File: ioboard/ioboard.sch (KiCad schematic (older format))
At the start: 18 parts

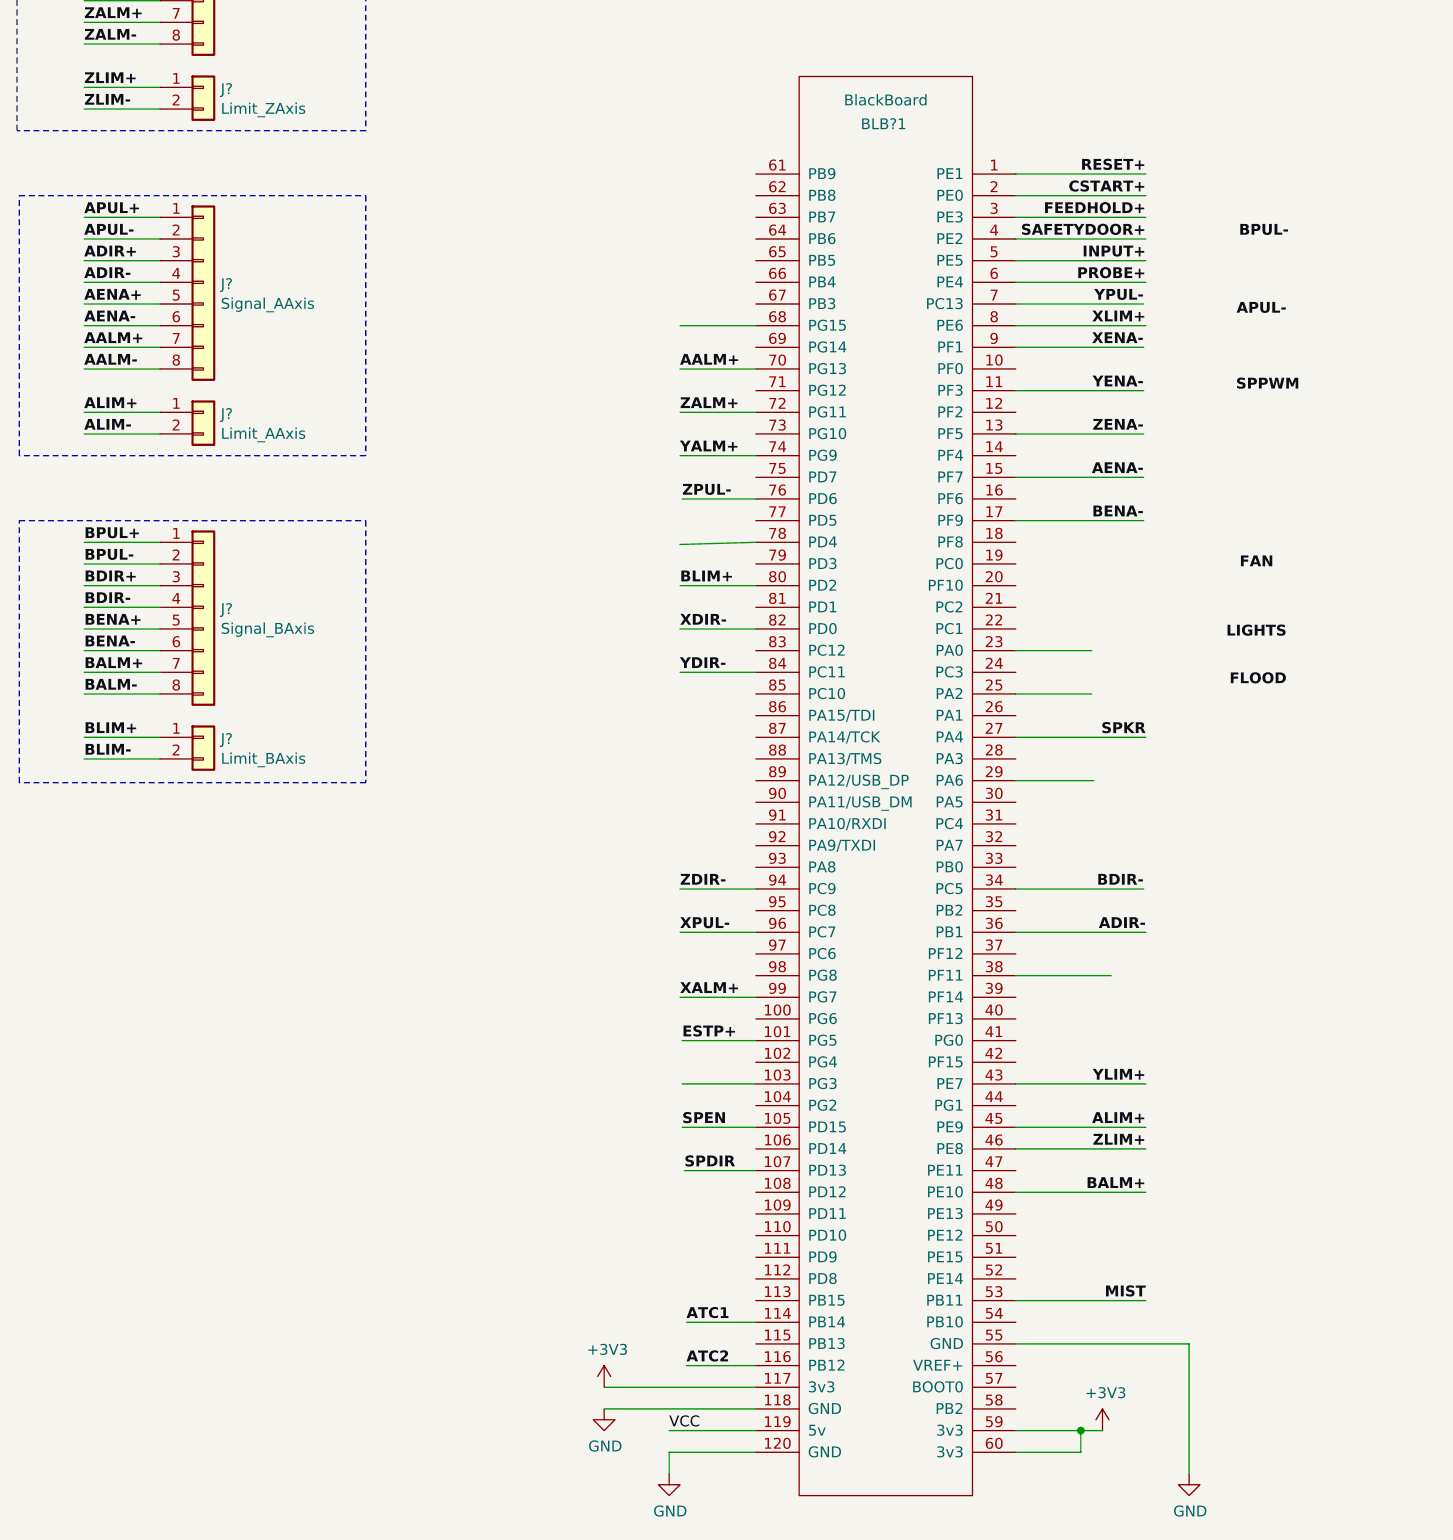
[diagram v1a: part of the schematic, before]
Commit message: system.stm32.[ch] has been ported and now compiles
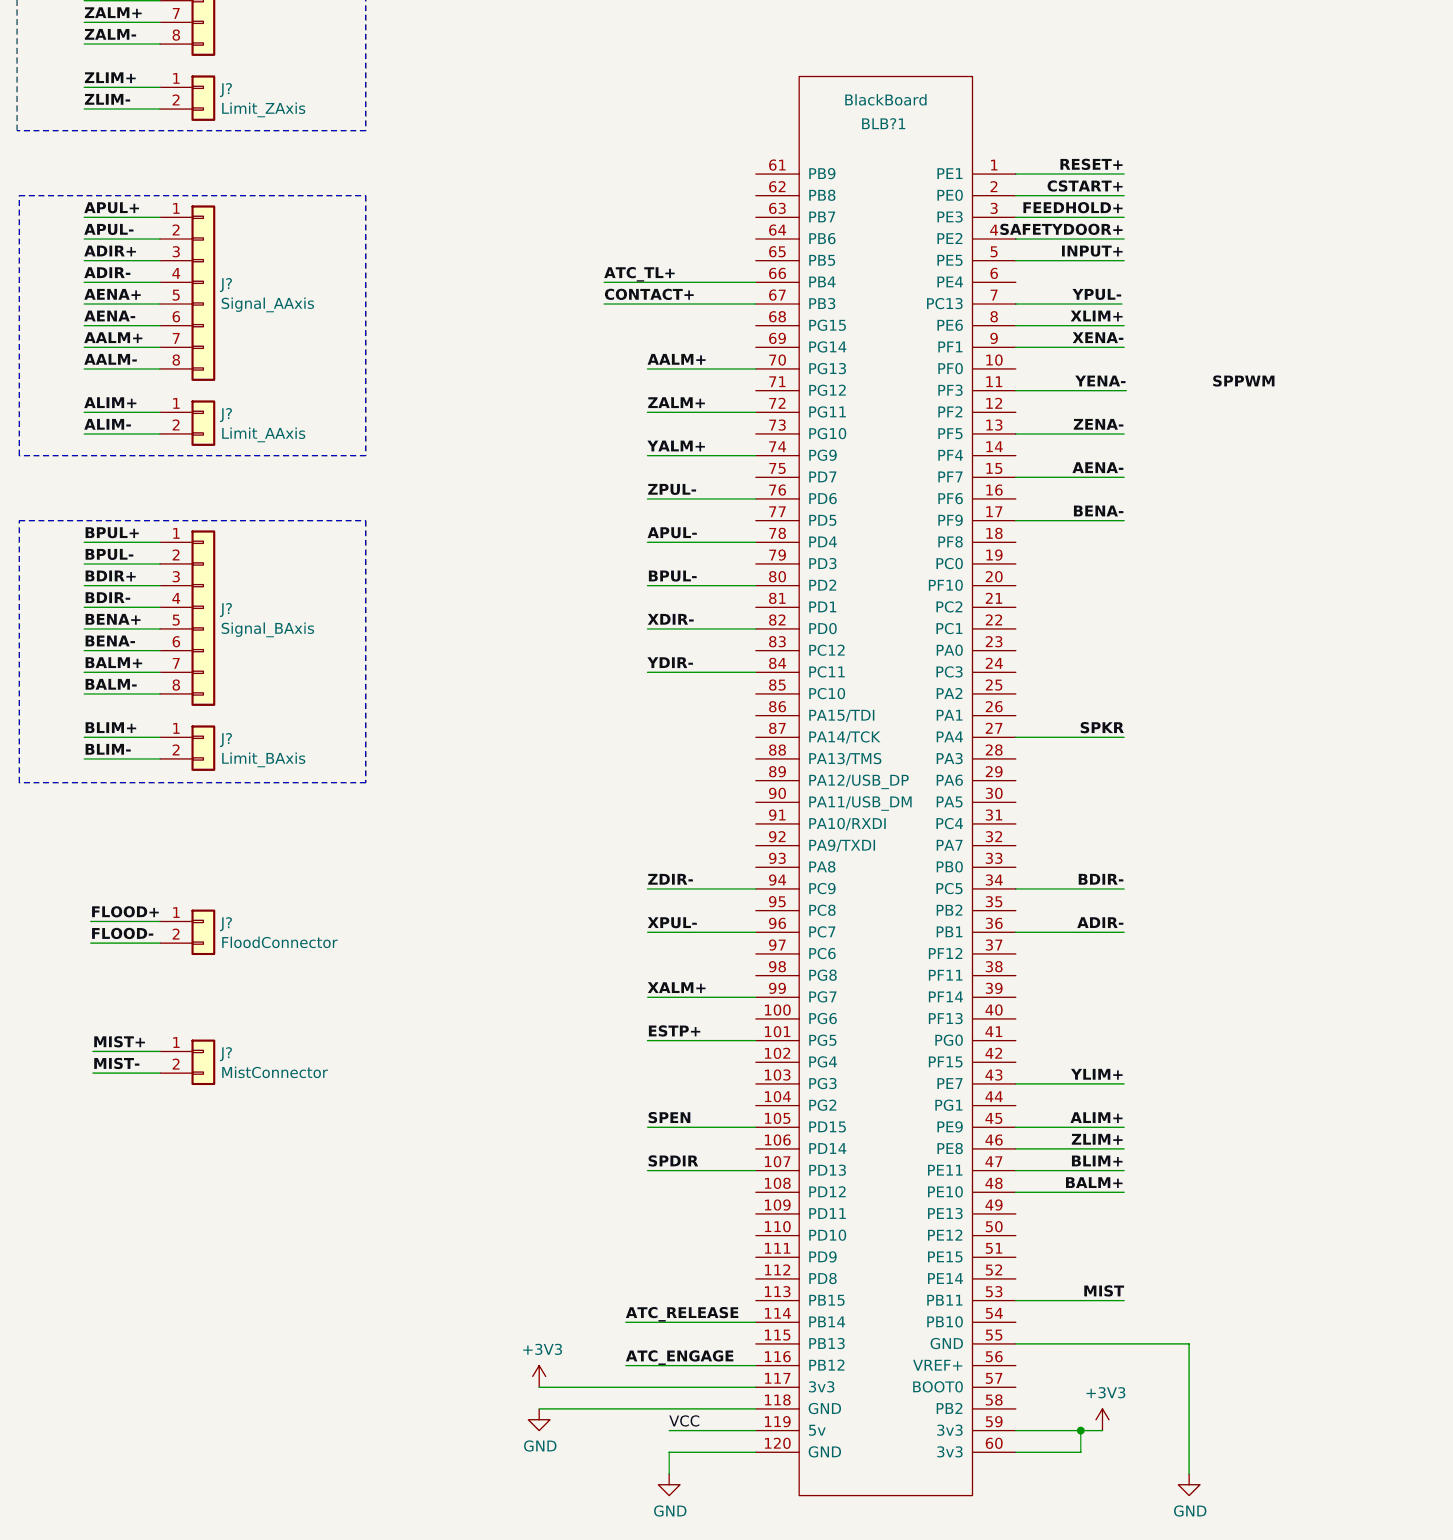
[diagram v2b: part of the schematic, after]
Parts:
- added J?: FloodConnector, symbol Connector_Generic:Conn_01x02
- added J?: MistConnector, symbol Connector_Generic:Conn_01x02
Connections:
- net labels added: ATC_ENGAGE, ATC_RELEASE, ATC_TL+, CONTACT+, FLOOD+, FLOOD-, MIST+, MIST-
- net labels removed: ATC1, ATC2, FAN, FLOOD, LIGHTS, PROBE+
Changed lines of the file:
@@
 L power:GND #PWR?
 U 1 1 606A4231
-P 4100 11500
-F 0 "#PWR?" H 4100 11250 50  0001 C CNN
-F 1 "GND" H 4105 11327 50  0000 C CNN
-F 2 "" H 4100 11500 50  0001 C CNN
-F 3 "" H 4100 11500 50  0001 C CNN
-	1    4100 11500
+P 3800 11500
+F 0 "#PWR?" H 3800 11250 50  0001 C CNN
+F 1 "GND" H 3805 11327 50  0000 C CNN
+F 2 "" H 3800 11500 50  0001 C CNN
+F 3 "" H 3800 11500 50  0001 C CNN
+	1    3800 11500
 	1    0    0    -1
 $EndComp
@@
 	5050 1640 4700 1640
 Wire Wire Line
-	4800 7900 4450 7900
+	4800 7900 4300 7900
 Wire Wire Line
 	5050 1540 4700 1540
 Wire Wire Line
-	4800 9300 4450 9300
+	4800 9300 4300 9300
 Wire Wire Line
 	5050 1440 4700 1440
-Text Label 4450 9300 0    50   ~ 10
+Text Label 4300 9300 0    50   ~ 10
 XPUL-
-Text Label 4450 7900 0    50   ~ 10
+Text Label 4300 7900 0    50   ~ 10
 XDIR-
 Text Label 5600 1200 0    50   ~ 10
@@
 	5050 2140 4700 2140
 Wire Wire Line
-	4800 8100 4450 8100
+	4800 8100 4300 8100
 Wire Wire Line
 	5050 2040 4700 2040
 Wire Wire Line
 	5050 1940 4700 1940
-Text Label 4450 8100 0    50   ~ 10
+Text Label 4300 8100 0    50   ~ 10
 YDIR-
-Text Label 4450 7100 0    50   ~ 10
+Text Label 4300 7100 0    50   ~ 10
 YALM+
 Text Label 5600 1400 0    50   ~ 10
@@
 	6000 1600 5600 1600
 Wire Wire Line
-	4800 9100 4450 9100
+	4800 9100 4300 9100
 Wire Wire Line
 	5050 2540 4700 2540
-Text Label 4450 9100 0    50   ~ 10
+Text Label 4300 9100 0    50   ~ 10
 ZDIR-
-Text Label 4450 6900 0    50   ~ 10
+Text Label 4300 6900 0    50   ~ 10
 ZALM+
 Text Label 5600 1600 0    50   ~ 10
@@
 	5050 3150 4700 3150
 Wire Wire Line
-	6000 9300 6600 9300
+	6000 9300 6500 9300
 Wire Wire Line
 	5050 3050 4700 3050
 Wire Wire Line
-	6000 6000 6600 6000
+	6000 6000 6500 6000
 Wire Wire Line
 	5050 2940 4700 2940
-Text Label 7250 6460 2    50   ~ 10
+Text Label 4300 7500 0    50   ~ 10
 APUL-
-Text Label 6600 9300 2    50   ~ 10
+Text Label 6500 9300 2    50   ~ 10
 ADIR-
 Wire Wire Line
@@
 	5050 3640 4700 3640
 Wire Wire Line
-	6000 9100 6590 9100
+	6000 9100 6500 9100
 Wire Wire Line
 	5050 3540 4700 3540
 Wire Wire Line
-	6000 5800 6600 5800
+	6000 5800 6500 5800
 Wire Wire Line
 	5050 3450 4700 3450
-Text Label 7260 6100 2    50   ~ 10
+Text Label 4300 7700 0    50   ~ 10
 BPUL-
-Text Label 6590 9100 2    50   ~ 10
+Text Label 6500 9100 2    50   ~ 10
 BDIR-
 Text Label 5600 2000 0    50   ~ 10
@@
 	14600 2100 13550 2100
 Connection ~ 13550 2100
-Text Label 4450 9600 0    50   ~ 10
+Text Label 4300 9600 0    50   ~ 10
 XALM+
-Text Label 6590 6400 2    50   ~ 10
+Text Label 6490 6400 2    50   ~ 10
 YPUL-
 Wire Wire Line
-	6000 6400 6590 6400
-Text Label 7310 6810 2    50   ~ 10
+	6000 6400 6490 6400
+Text Label 7200 6800 2    50   ~ 10
 SPPWM
 Wire Wire Line
-	6000 6200 6600 6200
-Text Label 6590 6600 2    50   ~ 10
+	6000 6200 6500 6200
+Text Label 6500 6600 2    50   ~ 10
 XENA-
-Text Label 6590 6800 2    50   ~ 10
+Text Label 6510 6800 2    50   ~ 10
 YENA-
-Text Label 6590 7000 2    50   ~ 10
+Text Label 6500 7000 2    50   ~ 10
 ZENA-
-Text Label 6590 7200 2    50   ~ 10
+Text Label 6500 7200 2    50   ~ 10
 AENA-
-Text Label 6590 7400 2    50   ~ 10
+Text Label 6500 7400 2    50   ~ 10
 BENA-
 Text Label 4400 11600 0    50   ~ 0
@@
 	4400 11700 4400 11800
 Wire Wire Line
-	4100 11500 4800 11500
+	3800 11500 4800 11500
 Wire Wire Line
 	6000 11200 6800 11200
@@
 	6800 11200 6800 11800
 Wire Wire Line
-	6000 6600 6590 6600
-Wire Wire Line
-	6000 6800 6590 6800
-Wire Wire Line
-	6000 7000 6590 7000
-Wire Wire Line
-	6000 7200 6590 7200
-Wire Wire Line
-	6000 7400 6590 7400
+	6000 6600 6500 6600
+Wire Wire Line
+	6000 6800 6510 6800
+Wire Wire Line
+	6000 7000 6500 7000
+Wire Wire Line
+	6000 7200 6500 7200
+Wire Wire Line
+	6000 7400 6500 7400
 $Comp
 L power:VCC #PWR?
@@
 Connection ~ 5050 1440
 Wire Wire Line
-	4450 6900 4800 6900
-Wire Wire Line
-	4450 7100 4800 7100
-Wire Wire Line
-	4450 9600 4800 9600
+	4300 6900 4800 6900
+Wire Wire Line
+	4300 7100 4800 7100
+Wire Wire Line
+	4300 9600 4800 9600
 $Comp
 L Connector_Generic:Conn_01x02 J?
@@
 L power:+3V3 #PWR?
 U 1 1 60FA9E2C
-P 4100 11400
-F 0 "#PWR?" H 4100 11250 50  0001 C CNN
-F 1 "+3V3" H 4115 11573 50  0000 C CNN
-F 2 "" H 4100 11400 50  0001 C CNN
-F 3 "" H 4100 11400 50  0001 C CNN
-	1    4100 11400
-	1    0    0    -1
-$EndComp
-Wire Wire Line
-	4100 11400 4800 11400
+P 3800 11400
+F 0 "#PWR?" H 3800 11250 50  0001 C CNN
+F 1 "+3V3" H 3815 11573 50  0000 C CNN
+F 2 "" H 3800 11400 50  0001 C CNN
+F 3 "" H 3800 11400 50  0001 C CNN
+	1    3800 11400
+	1    0    0    -1
+$EndComp
+Wire Wire Line
+	3800 11400 4800 11400
 $Comp
 L power:+3V3 #PWR?
@@
 Wire Wire Line
 	6000 2200 6000 2390
-Text Label 4460 9800 0    50   ~ 10
+Text Label 4300 9800 0    50   ~ 10
 ESTP+
 Wire Wire Line
-	4800 9800 4460 9800
+	4800 9800 4300 9800
 $Comp
 L Connector_Generic:Conn_01x02 J?
@@
 Wire Wire Line
 	9300 4000 9800 4000
-Text Label 6600 6500 2    50   ~ 10
+Text Label 6500 6500 2    50   ~ 10
 XLIM+
-Text Label 6600 10000 2    50   ~ 10
+Text Label 6500 10000 2    50   ~ 10
 YLIM+
-Text Label 6600 10300 2    50   ~ 10
+Text Label 6500 10300 2    50   ~ 10
 ZLIM+
-Text Label 6600 5800 2    50   ~ 10
+Text Label 6500 5800 2    50   ~ 10
 RESET+
-Text Label 6600 6000 2    50   ~ 10
+Text Label 6500 6000 2    50   ~ 10
 FEEDHOLD+
-Text Label 6600 5900 2    50   ~ 10
+Text Label 6500 5900 2    50   ~ 10
 CSTART+
 Wire Wire Line
-	6350 8000 6000 8000
-Wire Wire Line
-	6350 8200 6000 8200
-Wire Wire Line
-	6600 8400 6000 8400
-Text Label 6600 6300 2    50   ~ 10
-PROBE+
-Wire Wire Line
-	6360 8600 6000 8600
-Text Label 7190 7630 2    50   ~ 10
-FAN
-Text Label 7250 7950 2    50   ~ 10
-LIGHTS
-Text Label 7250 8170 2    50   ~ 10
-FLOOD
-Text Label 6600 11000 2    50   ~ 10
+	6500 8400 6000 8400
+Text Label 4100 6300 0    50   ~ 10
+ATC_TL+
+Text Label 6500 11000 2    50   ~ 10
 MIST
 Wire Wire Line
-	6600 11000 6000 11000
-Text Label 4460 10200 0    50   ~ 10
+	6500 11000 6000 11000
+Text Label 4300 10200 0    50   ~ 10
 SPEN
 Wire Wire Line
-	4460 10200 4800 10200
-Text Label 4470 10400 0    50   ~ 10
+	4300 10200 4800 10200
+Text Label 4300 10400 0    50   ~ 10
 SPDIR
 Wire Wire Line
-	4800 10400 4470 10400
-Text Label 4460 7300 0    50   ~ 10
+	4800 10400 4300 10400
+Text Label 4300 7300 0    50   ~ 10
 ZPUL-
 Wire Wire Line
-	4460 7300 4800 7300
-Wire Wire Line
-	6440 9500 6000 9500
-Text Label 6600 8400 2    50   ~ 10
+	4300 7300 4800 7300
+Text Label 6500 8400 2    50   ~ 10
 SPKR
-Text Label 4480 11300 0    50   ~ 10
-ATC2
-Wire Wire Line
-	4480 11300 4800 11300
-Text Label 4480 11100 0    50   ~ 10
-ATC1
-Wire Wire Line
-	4480 11100 4800 11100
+Text Label 4200 11300 0    50   ~ 10
+ATC_ENGAGE
+Wire Wire Line
+	4200 11300 4800 11300
+Text Label 4200 11100 0    50   ~ 10
+ATC_RELEASE
+Wire Wire Line
+	4200 11100 4800 11100
 Wire Wire Line
 	2050 6700 1700 6700
@@
 AALM+
 Wire Wire Line
-	4450 6700 4800 6700
-Wire Wire Line
-	4450 6500 4800 6500
-Text Label 4450 6700 0    50   ~ 10
+	4300 6700 4800 6700
+Text Label 4300 6700 0    50   ~ 10
 AALM+
-Text Label 6600 10500 2    50   ~ 10
+Text Label 6500 10500 2    50   ~ 10
 BALM+
-Wire Wire Line
-	4800 7500 4450 7510
-Wire Wire Line
-	4450 7700 4800 7700
-Text Label 6600 6200 2    50   ~ 10
+Text Label 6500 6200 2    50   ~ 10
 INPUT+
 Wire Wire Line
-	4460 10000 4800 10000
-Wire Wire Line
-	6600 5900 6000 5900
-Text Label 6600 6100 2    50   ~ 10
+	6500 5900 6000 5900
+Text Label 6500 6100 2    50   ~ 10
 SAFETYDOOR+
 Wire Wire Line
-	6600 6100 6000 6100
-Wire Wire Line
-	6600 6500 6000 6500
-Wire Wire Line
-	6600 6300 6000 6300
-Wire Wire Line
-	6600 10000 6000 10000
-Wire Wire Line
-	6600 10300 6000 10300
-Text Label 6600 10200 2    50   ~ 10
+	6500 6100 6000 6100
+Wire Wire Line
+	6500 6500 6000 6500
+Wire Wire Line
+	6500 10000 6000 10000
+Wire Wire Line
+	6500 10300 6000 10300
+Text Label 6500 10200 2    50   ~ 10
 ALIM+
-Text Label 4450 7700 0    50   ~ 10
+Text Label 6500 10400 2    50   ~ 10
 BLIM+
+Wire Wire Line
+	6500 10500 6000 10500
+Wire Wire Line
+	6500 10200 6000 10200
+Wire Wire Line
+	4800 6300 4100 6300
+Wire Wire Line
+	4800 7500 4300 7500
+Wire Wire Line
+	6000 10400 6500 10400
 $Comp
 L STM32Boards:BlackBoard BLB?1
@@
 $EndComp
 Wire Wire Line
-	6600 10500 6000 10500
-Wire Wire Line
-	6600 10200 6000 10200
+	4800 7700 4300 7700
+Text Label 4100 6400 0    50   ~ 10
+CONTACT+
+Wire Wire Line
+	4100 6400 4800 6400
+$Comp
+L Connector_Generic:Conn_01x02 J?
+U 1 1 6125BAD7
+P 2250 9250
+F 0 "J?" H 2330 9242 50  0000 L CNN
+F 1 "FloodConnector" H 2330 9151 50  0000 L CNN
+F 2 "" H 2250 9250 50  0001 C CNN
+F 3 "~" H 2250 9250 50  0001 C CNN
+	1    2250 9250
+	1    0    0    -1
+$EndComp
+$Comp
+L Connector_Generic:Conn_01x02 J?
+U 1 1 6125CD13
+P 2250 9850
+F 0 "J?" H 2330 9842 50  0000 L CNN
+F 1 "MistConnector" H 2330 9751 50  0000 L CNN
+F 2 "" H 2250 9850 50  0001 C CNN
+F 3 "~" H 2250 9850 50  0001 C CNN
+	1    2250 9850
+	1    0    0    -1
+$EndComp
+Text Label 1730 9250 0    50   ~ 10
+FLOOD+
+Text Label 1730 9350 0    50   ~ 10
+FLOOD-
+Wire Wire Line
+	2050 9250 1730 9250
+Wire Wire Line
+	2050 9350 1730 9350
+Text Label 1740 9850 0    50   ~ 10
+MIST+
+Text Label 1740 9950 0    50   ~ 10
+MIST-
+Wire Wire Line
+	2050 9850 1740 9850
+Wire Wire Line
+	2050 9950 1740 9950
 $EndSCHEMATC
